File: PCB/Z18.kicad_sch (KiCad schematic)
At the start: 193 parts, among them J1 C165948_-_USB_C_Receptacle_US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, J2 SM02B-SRSS-TB(LF)(SN), J3 SM02B-SRSS-TB(LF)(SN), J4 Conn_ARM_JTAG_SWD_10, Q1 Q_PMOS_GSD, SW1 CAP_STP, SW10 A, SW11 WIN_1.25U, SW12 2, SW13 W, SW14 S, SW15 Z, SW16 L_ALT_1.25U, SW17 L_ALT_1.5U, SW18 3, SW19 E, SW2 ESC, SW20 D, SW21 X, SW22 4, SW23 R, SW24 F, SW25 C, SW26 5, SW27 T, SW28 G, SW29 V, SW3 Tab, SW30 SPC_6.25U, SW31 SPC_7U, SW32 6, SW33 Y, SW34 H, SW35 B, SW36 7, SW37 U, SW38 J, SW39 N, SW4 CAP, SW40 8, SW41 I, SW42 K, SW43 M, SW44 R_ALT_1U, SW45 R_ALT_1.5U, SW46 9, SW47 O, SW48 L, SW49 ,, SW5 L_SHFT, SW50 R_WIN_1U, SW51 R_CTRL_1.5U, SW52 0, SW53 P, SW54 ;, SW55 ., SW56 R_CTRL_1U, SW57 -, SW58 [, SW59 ', SW6 L_CTRL_1.25U, SW60 /, SW61 =, SW62 ], SW63 R_SHFT_1.75U, SW64 LEFT, SW65 Rotary_Encoder_Switch-Device-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, SW66 BCKSP, SW67 \, SW68 ENT, SW69 UP, SW7 L_CTRL_1.5U, SW70 DOWN, SW71 ENT_ISO, SW72 Tilde, SW73 Del, SW74 PG_UP, SW75 PG_DWN, SW76 RIGHT, SW77 ISO_SPARE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

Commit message: starting updates, incomplete
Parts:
- removed C1, C3: 10uF, Capacitor_SMD:C_0603_1608Metric, symbol Device:C_Small
- added D? (x13): D, Diode_SMD:D_SOD-123, symbol Device:D_Small
- added SW?: np_9, Button_Switch_Keyboard:SW_Cherry_MX_1.00u_PCB, symbol Switch:SW_Push
- added SW?: np_0, Button_Switch_Keyboard:SW_Cherry_MX_1.00u_PCB, symbol Switch:SW_Push
- added SW?: np_minus, Button_Switch_Keyboard:SW_Cherry_MX_1.00u_PCB, symbol Switch:SW_Push
- added SW?: np_3, Button_Switch_Keyboard:SW_Cherry_MX_1.00u_PCB, symbol Switch:SW_Push
- added SW?: np_5, Button_Switch_Keyboard:SW_Cherry_MX_1.00u_PCB, symbol Switch:SW_Push
- added SW?: np_ent, Button_Switch_Keyboard:SW_Cherry_MX_1.00u_PCB, symbol Switch:SW_Push
- added SW?: np_2, Button_Switch_Keyboard:SW_Cherry_MX_1.00u_PCB, symbol Switch:SW_Push
- added SW?: np_plus, Button_Switch_Keyboard:SW_Cherry_MX_1.00u_PCB, symbol Switch:SW_Push
- added SW?: np_/, Button_Switch_Keyboard:SW_Cherry_MX_1.00u_PCB, symbol Switch:SW_Push
- added SW?: np_dot, Button_Switch_Keyboard:SW_Cherry_MX_1.00u_PCB, symbol Switch:SW_Push
- added SW?: np_6, Button_Switch_Keyboard:SW_Cherry_MX_1.00u_PCB, symbol Switch:SW_Push
- added SW?: np_8, Button_Switch_Keyboard:SW_Cherry_MX_1.00u_PCB, symbol Switch:SW_Push
- added SW?: np_star, Button_Switch_Keyboard:SW_Cherry_MX_1.00u_PCB, symbol Switch:SW_Push
- SW72: value Tilde -> np_del
- SW74: value PG_UP -> np_4
- SW75: value PG_DWN -> np1
- U3: footprint RF_Module:Raytac_MDBT50Q -> COBoards:E73-2G4M08S1C; symbol RF_Module:MDBT50Q-1MV2 -> COBoards:E73-2G4M08S1C; LCSC PN (none) -> C356849; Manufacturer PN (none) -> E73-2G4M08S1C
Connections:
- net BATTERY_MEASURE: no longer U3.20 (P0.04/AIN2)
- net BOOT_LED: no longer U3.50 (P1.02)
- net Col0: no longer U3.3 (P1.10)
- net Col1: no longer U3.4 (P1.11)
- net Col10: no longer U3.13 (P0.28/AIN4)
- net Col11: no longer U3.14 (P0.30/AIN6)
- net Col12: no longer U3.22 (P0.06)
- net Col13: no longer U3.24 (P0.08)
- net Col14: no longer U3.26 (TRACEDATA3/P1.09)
- net Col2: no longer U3.5 (P1.12)
- net Col3: no longer U3.6 (P1.13)
- net Col4: no longer U3.7 (P1.14)
- net Col5: no longer U3.8 (P1.15)
- net Col6: no longer U3.9 (P0.03/AIN1)
- net Col7: no longer U3.10 (P0.29/AIN5)
- net Col8: no longer U3.11 (P0.02/AIN0)
- net Col9: no longer U3.12 (P0.31/AIN7)
- net D+: now also U3.31 (D+)
- net D-: now also U3.29 (D-)
- net GND: now also U3.21 (GND), U3.24 (GND); no longer U3.1 (GND), U3.15 (GND), U3.2 (GND), U3.33 (GND), U3.55 (GND)
- net RESET: now also U3.26 (P0.18/RESET); no longer U3.40 (~RESET~/P0.18)
- net Row0: now also D?.1 (K), D?.1 (K), D?.1 (K); no longer U3.60 (P1.03)
- net Row1: now also D?.1 (K), D?.1 (K), D?.1 (K); no longer U3.59 (P1.05)
- net Row2: now also D?.1 (K), D?.1 (K); no longer U3.58 (P1.07)
- net Row3: now also D?.1 (K), D?.1 (K), D?.1 (K); no longer U3.57 (P1.06)
- net Row4: now also D?.1 (K), D?.1 (K); no longer U3.56 (P1.04)
- net SWC: now also U3.39 (SWDCLK); no longer U3.53 (SWDCLK)
- net SWD: now also U3.37 (SWDIO); no longer U3.51 (SWDIO)
- net VBUS: now also U3.27 (VBUS); no longer U3.32 (VBUS)
- net VDD: now also U3.19 (VDD), U3.23 (VDDH); no longer U3.28 (VDD), U3.30 (VDDH)
- net at R9.2: no longer U3.34 (D-)
- net at C6.2, Y1.1: now also U3.13 (P0.01/XL2); no longer U3.17 (XL1/P0.00)
- net at C7.2, Y1.2: now also U3.11 (P0.00/XL1); no longer U3.18 (XL2/P0.01)
- net DCCH: now reaches U3.25 (DCCH)
- net at U3.35 (P0.24): no longer R10.2
- net at U3.41 (P0.09/NFC1): no longer TP1.1
- net at TP2.1: no longer U3.44 (P0.20)
- net at TP3.1: no longer U3.46 (P0.22)
- new net: D?.2 (A), SW?.2 (x13)
- new net Col15: SW?.1, SW?.1, SW?.1, SW?.1, SW?.1
- new net Col16: SW?.1, SW?.1, SW?.1, SW?.1, SW?.1
- new net Col17: SW?.1, SW?.1, SW?.1
- no-connect marks 34 -> 20
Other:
- moved on the sheet: BATT1, C2, C5, C6, C7, D1, D2, J1, Q1, R11, R3, R4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

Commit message: layout and routing in progress, ~70% complete
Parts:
- removed D72: D, Diode_SMD:D_SOD-123, symbol Device:D_Small
- removed H2, H3, H4, H5: MountingHole_Pad, MountingHole:MountingHole_2.2mm_M2, symbol Mechanical:MountingHole_Pad
- removed J4: Conn_ARM_JTAG_SWD_10, Connector:Tag-Connect_TC2030-IDC-NL_2x03_P1.27mm_Vertical, symbol Connector:Conn_ARM_JTAG_SWD_10
- removed R10, R9: 27R, Resistor_SMD:R_0603_1608Metric, symbol Device:R_Small
- removed SW31: SPC_7U, COBoards:MX_7U, symbol Switch:SW_Push
- removed SW65: Rotary_Encoder_Switch-Device-SofleKeyboard-rescue, symbol COBoards:Rotary_Encoder_Switch-Device-SofleKeyboard-rescue
- removed SW71: ENT_ISO, Button_Switch_Keyboard:SW_Cherry_MX_ISOEnter_PCB, symbol Switch:SW_Push
- removed SW77: ISO_SPARE, Button_Switch_Keyboard:SW_Cherry_MX_1.00u_PCB, symbol Switch:SW_Push
- removed TP1, TP2, TP3: TestPoint, TestPoint:TestPoint_Pad_1.0x1.0mm, symbol Connector:TestPoint
- added H13: MountingHole_Pad, MountingHole:MountingHole_4.3mm_M4, symbol Mechanical:MountingHole_Pad
- added J5: Conn_01x04_Male, Connector_PinHeader_2.54mm:PinHeader_1x04_P2.54mm_Vertical, symbol Connector:Conn_01x04_Male
- SW1: renamed from SW2; footprint Button_Switch_Keyboard:SW_Cherry_MX_1.00u_PCB -> COBoards:MX_1U
- SW10: renamed from SW46; footprint Button_Switch_Keyboard:SW_Cherry_MX_1.00u_PCB -> COBoards:MX_1U
- SW11: renamed from SW52; footprint Button_Switch_Keyboard:SW_Cherry_MX_1.00u_PCB -> COBoards:MX_1U
- SW12: renamed from SW57; footprint Button_Switch_Keyboard:SW_Cherry_MX_1.00u_PCB -> COBoards:MX_1U
- SW13: renamed from SW61; footprint Button_Switch_Keyboard:SW_Cherry_MX_1.00u_PCB -> COBoards:MX_1U
- SW14: renamed from SW66; footprint Button_Switch_Keyboard:SW_Cherry_MX_2.00u_PCB -> COBoards:MX_2U
- SW15: renamed from SW72; footprint Button_Switch_Keyboard:SW_Cherry_MX_1.00u_PCB -> COBoards:MX_1U
- SW16, SW17, SW18, SW34, SW35, SW54, SW55, SW70, SW71, SW83, SW84: renamed from SW?; footprint Button_Switch_Keyboard:SW_Cherry_MX_1.00u_PCB -> COBoards:MX_1U
- SW19: renamed from SW3; footprint Button_Switch_Keyboard:SW_Cherry_MX_1.50u_PCB -> COBoards:MX_1.5U
- SW2: renamed from SW8; footprint Button_Switch_Keyboard:SW_Cherry_MX_1.00u_PCB -> COBoards:MX_1U
- SW20: renamed from SW9; footprint Button_Switch_Keyboard:SW_Cherry_MX_1.00u_PCB -> COBoards:MX_1U
- SW21: renamed from SW13; footprint Button_Switch_Keyboard:SW_Cherry_MX_1.00u_PCB -> COBoards:MX_1U
- SW22: renamed from SW19; footprint Button_Switch_Keyboard:SW_Cherry_MX_1.00u_PCB -> COBoards:MX_1U
- SW23, SW48: footprint Button_Switch_Keyboard:SW_Cherry_MX_1.00u_PCB -> COBoards:MX_1U
- SW24: renamed from SW27; footprint Button_Switch_Keyboard:SW_Cherry_MX_1.00u_PCB -> COBoards:MX_1U
- SW25: renamed from SW33; footprint Button_Switch_Keyboard:SW_Cherry_MX_1.00u_PCB -> COBoards:MX_1U
- SW26: renamed from SW37; footprint Button_Switch_Keyboard:SW_Cherry_MX_1.00u_PCB -> COBoards:MX_1U
- SW27: renamed from SW41; footprint Button_Switch_Keyboard:SW_Cherry_MX_1.00u_PCB -> COBoards:MX_1U
- SW28: renamed from SW47; footprint Button_Switch_Keyboard:SW_Cherry_MX_1.00u_PCB -> COBoards:MX_1U
- SW29: renamed from SW53; footprint Button_Switch_Keyboard:SW_Cherry_MX_1.00u_PCB -> COBoards:MX_1U
- SW3: renamed from SW12; footprint Button_Switch_Keyboard:SW_Cherry_MX_1.00u_PCB -> COBoards:MX_1U
- SW30: renamed from SW58; footprint Button_Switch_Keyboard:SW_Cherry_MX_1.00u_PCB -> COBoards:MX_1U
- SW31: renamed from SW62; footprint Button_Switch_Keyboard:SW_Cherry_MX_1.00u_PCB -> COBoards:MX_1U
- SW32: renamed from SW67; footprint Button_Switch_Keyboard:SW_Cherry_MX_1.50u_PCB -> COBoards:MX_1.5U
- SW33: renamed from SW73; value Del -> np_7; footprint Button_Switch_Keyboard:SW_Cherry_MX_1.00u_PCB -> COBoards:MX_1U
- SW36, SW72: renamed from SW?; footprint Button_Switch_Keyboard:SW_Cherry_MX_1.00u_PCB -> COBoards:MX_2U
- SW39: renamed from SW4; footprint Button_Switch_Keyboard:SW_Cherry_MX_1.75u_PCB -> COBoards:MX_1.75U
- SW4: renamed from SW18; footprint Button_Switch_Keyboard:SW_Cherry_MX_1.00u_PCB -> COBoards:MX_1U
- SW40: renamed from SW10; footprint Button_Switch_Keyboard:SW_Cherry_MX_1.00u_PCB -> COBoards:MX_1U
- SW41: renamed from SW14; footprint Button_Switch_Keyboard:SW_Cherry_MX_1.00u_PCB -> COBoards:MX_1U
- SW42: renamed from SW20; footprint Button_Switch_Keyboard:SW_Cherry_MX_1.00u_PCB -> COBoards:MX_1U
- SW43: renamed from SW24; footprint Button_Switch_Keyboard:SW_Cherry_MX_1.00u_PCB -> COBoards:MX_1U
- SW44: renamed from SW28; footprint Button_Switch_Keyboard:SW_Cherry_MX_1.00u_PCB -> COBoards:MX_1U
- SW45: renamed from SW34; footprint Button_Switch_Keyboard:SW_Cherry_MX_1.00u_PCB -> COBoards:MX_1U
- SW46: renamed from SW38; footprint Button_Switch_Keyboard:SW_Cherry_MX_1.00u_PCB -> COBoards:MX_1U
- SW47: renamed from SW42; footprint Button_Switch_Keyboard:SW_Cherry_MX_1.00u_PCB -> COBoards:MX_1U
- SW49: renamed from SW54; footprint Button_Switch_Keyboard:SW_Cherry_MX_1.00u_PCB -> COBoards:MX_1U
- SW5: renamed from SW22; footprint Button_Switch_Keyboard:SW_Cherry_MX_1.00u_PCB -> COBoards:MX_1U
- SW50: renamed from SW59; footprint Button_Switch_Keyboard:SW_Cherry_MX_1.00u_PCB -> COBoards:MX_1U
- SW52: renamed from SW68; footprint Button_Switch_Keyboard:SW_Cherry_MX_2.25u_PCB -> COBoards:MX_2.25U
- SW53: renamed from SW74; footprint Button_Switch_Keyboard:SW_Cherry_MX_1.00u_PCB -> COBoards:MX_1U
- SW56: renamed from SW5; footprint Button_Switch_Keyboard:SW_Cherry_MX_2.25u_PCB -> COBoards:MX_2.25U
- SW57: renamed from SW15; footprint Button_Switch_Keyboard:SW_Cherry_MX_1.00u_PCB -> COBoards:MX_1U
- SW58: renamed from SW21; footprint Button_Switch_Keyboard:SW_Cherry_MX_1.00u_PCB -> COBoards:MX_1U
- SW59: renamed from SW25; footprint Button_Switch_Keyboard:SW_Cherry_MX_1.00u_PCB -> COBoards:MX_1U
- SW6: renamed from SW26; footprint Button_Switch_Keyboard:SW_Cherry_MX_1.00u_PCB -> COBoards:MX_1U
- SW60: renamed from SW29; footprint Button_Switch_Keyboard:SW_Cherry_MX_1.00u_PCB -> COBoards:MX_1U
- SW61: renamed from SW35; footprint Button_Switch_Keyboard:SW_Cherry_MX_1.00u_PCB -> COBoards:MX_1U
- SW62: renamed from SW39; footprint Button_Switch_Keyboard:SW_Cherry_MX_1.00u_PCB -> COBoards:MX_1U
- SW63: renamed from SW43; footprint Button_Switch_Keyboard:SW_Cherry_MX_1.00u_PCB -> COBoards:MX_1U
- SW64: renamed from SW49; footprint Button_Switch_Keyboard:SW_Cherry_MX_1.00u_PCB -> COBoards:MX_1U
- SW65: renamed from SW55; footprint Button_Switch_Keyboard:SW_Cherry_MX_1.00u_PCB -> COBoards:MX_1U
- SW66: renamed from SW60; footprint Button_Switch_Keyboard:SW_Cherry_MX_1.00u_PCB -> COBoards:MX_1U
- SW67: renamed from SW63; footprint Button_Switch_Keyboard:SW_Cherry_MX_1.75u_PCB -> COBoards:MX_1.75U
- SW68: renamed from SW69; footprint Button_Switch_Keyboard:SW_Cherry_MX_1.00u_PCB -> COBoards:MX_1U
- SW69: renamed from SW75; footprint Button_Switch_Keyboard:SW_Cherry_MX_1.00u_PCB -> COBoards:MX_1U
- SW7: renamed from SW32; footprint Button_Switch_Keyboard:SW_Cherry_MX_1.00u_PCB -> COBoards:MX_1U
- SW73: renamed from SW6; footprint Button_Switch_Keyboard:SW_Cherry_MX_1.25u_PCB -> COBoards:MX_1.25U
- SW74: renamed from SW11; footprint Button_Switch_Keyboard:SW_Cherry_MX_1.25u_PCB -> COBoards:MX_1.25U
- SW75: renamed from SW16; footprint Button_Switch_Keyboard:SW_Cherry_MX_1.25u_PCB -> COBoards:MX_1.25U
- SW76: renamed from SW30; footprint Button_Switch_Keyboard:SW_Cherry_MX_6.25u_PCB -> COBoards:MX_6.25U
- SW77: renamed from SW44; footprint Button_Switch_Keyboard:SW_Cherry_MX_1.00u_PCB -> COBoards:MX_1U
- SW78: renamed from SW50; footprint Button_Switch_Keyboard:SW_Cherry_MX_1.00u_PCB -> COBoards:MX_1U
- SW79: renamed from SW56; footprint Button_Switch_Keyboard:SW_Cherry_MX_1.00u_PCB -> COBoards:MX_1U
- SW8: renamed from SW36; footprint Button_Switch_Keyboard:SW_Cherry_MX_1.00u_PCB -> COBoards:MX_1U
- SW80: renamed from SW64; footprint Button_Switch_Keyboard:SW_Cherry_MX_1.00u_PCB -> COBoards:MX_1U
- SW81: renamed from SW70; footprint Button_Switch_Keyboard:SW_Cherry_MX_1.00u_PCB -> COBoards:MX_1U
- SW82: renamed from SW76; footprint Button_Switch_Keyboard:SW_Cherry_MX_1.00u_PCB -> COBoards:MX_1U
- SW85: renamed from SW51; footprint Button_Switch_Keyboard:SW_Cherry_MX_1.50u_PCB -> COBoards:MX_1.5U
- SW86: renamed from SW7; footprint Button_Switch_Keyboard:SW_Cherry_MX_1.50u_PCB -> COBoards:MX_1.5U
- SW87: renamed from SW17; footprint Button_Switch_Keyboard:SW_Cherry_MX_1.50u_PCB -> COBoards:MX_1.5U
- SW9: renamed from SW40; footprint Button_Switch_Keyboard:SW_Cherry_MX_1.00u_PCB -> COBoards:MX_1U
- gave numbers to parts that had none: 13
- renumbered C6 to C1, C7 to C2, C4 to C3, C5 to C4, C2 to C5, D4 to D1, D44 to D10, D49 to D11, D54 to D12, D58 to D13, D62 to D14, D67 to D15, D5 to D19, D9 to D2, D10 to D20, D14 to D21, D19 to D22, D27 to D24, D32 to D25, D36 to D26, D40 to D27, D45 to D28, D50 to D29, D13 to D3, D55 to D30, D59 to D31, D63 to D32, D68 to D33, D6 to D37, D11 to D38, D15 to D39, D18 to D4, D20 to D40, D24 to D41, D28 to D42, D33 to D43, D37 to D44, D41 to D45, D51 to D47, D56 to D48, D22 to D5, D64 to D50, D69 to D51, D7 to D54, D16 to D55, D21 to D56, D25 to D57, D29 to D58, D34 to D59, D26 to D6, D38 to D60, D42 to D61, D47 to D62, D52 to D63, D57 to D64, D60 to D65, D65 to D66, D70 to D67, D31 to D7, D8 to D71, D12 to D72, D17 to D73, D30 to D74, D43 to D75, D48 to D76, D53 to D77, D61 to D78, D66 to D79, D35 to D8, D71 to D80, D3 to D83, D2 to D85, D1 to D86, D39 to D9, H9 to H10, H10 to H11, H6 to H3, H11 to H5, H8 to H7, H7 to H9, J1 to J4, R6 to R1, R1 to R2, R2 to R3, R8 to R4, R3 to R5, R4 to R6, R11 to R8, R5 to R9, SW1 to SW38, SW45 to SW89, U3 to U2, U2 to U3
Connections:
- net Col10 is gone; now on net Col5: SW11.1, SW29.1, SW49.1, SW65.1, SW79.1, SW85.1
- net Col11 is gone; now on net Col5: SW12.1, SW30.1, SW50.1, SW66.1
- net Col12 is gone; now on net Col6: SW13.1, SW31.1, SW67.1, SW80.1
- net Col13 is gone; now on net Col6: SW14.1, SW32.1, SW52.1, SW68.1, SW81.1
- net Col14 is gone; now on net Col7: SW15.1, SW33.1, SW53.1, SW69.1, SW82.1
- net Col15 is gone; now on net Col7: SW16.1, SW34.1, SW54.1, SW70.1, SW83.1
- net Col16 is gone; now on net Col8: SW17.1, SW35.1, SW55.1, SW71.1, SW84.1
- net Col17 is gone; now on net Col8: SW18.1, SW36.1, SW72.1
- net BATTERY_MEASURE: now also U2.10 (P0.30/AIN6_(LowFreq))
- net BOOT_LED: now also U2.9 (P0.31/AIN7_(LowFreq))
- net Col0: now also SW2.1, SW20.1, SW40.1, SW74.1, U2.1 (P1.11)
- net Col1: now also SW21.1, SW22.1, SW3.1, SW4.1, SW41.1, SW42.1, SW57.1, SW58.1, SW75.1, SW87.1, U2.2 (P1.10_(LowFreq)); no longer SW2.1, SW20.1, SW40.1, SW74.1
- net Col2: now also SW23.1, SW24.1, SW43.1, SW44.1, SW5.1, SW59.1, SW6.1, SW60.1, SW76.1, U2.3 (P0.03/AIN1_(LowFreq)); no longer SW21.1, SW3.1, SW41.1, SW57.1, SW75.1, SW87.1
- net Col3: now also SW25.1, SW26.1, SW45.1, SW46.1, SW61.1, SW62.1, SW7.1, SW8.1, U2.4 (P0.28/AIN4); no longer SW22.1, SW4.1, SW42.1, SW58.1
- net Col4: now also SW10.1, SW27.1, SW28.1, SW47.1, SW48.1, SW63.1, SW64.1, SW77.1, SW89.1, SW9.1, U2.6 (P1.13_(LowFreq)); no longer SW23.1, SW43.1, SW5.1, SW59.1
- net Col5: now also SW78.1, U2.8 (P0.29/AIN5_(LowFreq)); no longer SW24.1, SW44.1, SW6.1, SW60.1, SW76.1
- net Col6: now also U2.7 (P0.02/AIN0_(LowFreq)); no longer SW25.1, SW45.1, SW61.1, SW7.1
- net Col7: now also U2.15 (P0.05/AIN3); no longer SW26.1, SW46.1, SW62.1, SW8.1
- net Col8: now also U2.17 (P1.09); no longer SW27.1, SW47.1, SW63.1, SW77.1, SW89.1, SW9.1
- net GND: now also U2.5 (GND), J5.1 (Pin_1)
- net Row0: now also U2.43 (P0.10/NFC2)
- net Row1: now also U2.41 (P0.09/NFC1)
- net Row2: now also U2.35 (P0.24)
- net Row3: now also U2.33 (P0.13)
- net Row4: now also U2.12 (P0.26)
- net SWC: now also J5.4 (Pin_4)
- net SWD: now also J5.3 (Pin_3)
- removed net Col9: SW10.1, SW28.1, SW48.1, SW64.1, SW78.1
- no-connect marks 20 -> 26
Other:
- moved on the sheet: BATT1, C1, C2, C4, C5, D75, D76, D77, D85, D86, J3, J4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

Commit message: routed
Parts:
- removed SW86: L_CTRL_1.5U, COBoards:MX_1.5U, symbol Switch:SW_Push
- removed SW87: L_ALT_1.5U, COBoards:MX_1.5U, symbol Switch:SW_Push
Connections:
- net Col0: now also U2.2 (P1.10_(LowFreq)); no longer U2.1 (P1.11)
- net Col1: now also U2.1 (P1.11); no longer U2.2 (P1.10_(LowFreq))
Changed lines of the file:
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@@
     (stroke (width 0) (type solid) (color 0 0 0 0))
   )
-  (wire (pts (xy 46.99 114.3) (xy 46.99 102.87))
-    (stroke (width 0) (type solid) (color 0 0 0 0))
-  )
   (wire (pts (xy 200.66 40.64) (xy 200.66 55.88))
     (stroke (width 0) (type solid) (color 0 0 0 0))
@@
     (stroke (width 0) (type solid) (color 0 0 0 0))
   )
-  (wire (pts (xy 77.47 114.3) (xy 77.47 101.6))
-    (stroke (width 0) (type solid) (color 0 0 0 0))
-  )
   (wire (pts (xy 40.64 66.04) (xy 40.64 71.12))
     (stroke (width 0) (type solid) (color 0 0 0 0))
@@
     (stroke (width 0) (type solid) (color 0 0 0 0))
   )
-  (wire (pts (xy 87.63 101.6) (xy 87.63 114.3))
-    (stroke (width 0) (type solid) (color 0 0 0 0))
-  )
   (wire (pts (xy 71.12 142.24) (xy 71.12 139.7))
     (stroke (width 0) (type solid) (color 0 0 0 0))
@@
     (stroke (width 0) (type default) (color 0 0 0 0))
   )
-  (wire (pts (xy 57.15 101.6) (xy 57.15 114.3))
-    (stroke (width 0) (type solid) (color 0 0 0 0))
-  )
   (wire (pts (xy 185.42 86.36) (xy 185.42 101.6))
     (stroke (width 0) (type default) (color 0 0 0 0))
@@
     (effects (font (size 1.27 1.27)) (justify right bottom))
   )
-  (label "Col1" (at 85.09 220.98 0)
+  (label "Col1" (at 85.09 223.52 0)
     (effects (font (size 1.27 1.27)) (justify left bottom))
   )
@@
     (effects (font (size 1.27 1.27)) (justify left bottom))
   )
-  (label "Col0" (at 85.09 223.52 0)
+  (label "Col0" (at 85.09 220.98 0)
     (effects (font (size 1.27 1.27)) (justify left bottom))
   )
@@
     (pin "2")
   )
-  (symbol (lib_id "Switch:SW_Push") (at 52.07 114.3 0) (unit 1)
-    (in_bom yes) (on_board yes)
-    (property "Reference" "SW86" (id 0) (at 52.07 109.7088 0))
-    (property "Value" "L_CTRL_1.5U" (id 1) (at 50.165 112.008 0))
-    (property "Footprint" "COBoards:MX_1.5U" (id 2) (at 52.07 109.22 0)
-      (effects (font (size 1.27 1.27)) hide)
-    )
-    (property "Datasheet" "~" (id 3) (at 52.07 109.22 0)
-      (effects (font (size 1.27 1.27)) hide)
-    )
-    (pin "1")
-    (pin "2")
-  )
   (symbol (lib_id "COBoards:E73-2G4M08S1C") (at 57.15 210.82 0) (unit 1)
     (in_bom yes) (on_board yes)
@@
     (pin "2")
   )
-  (symbol (lib_id "Switch:SW_Push") (at 82.55 114.3 0) (unit 1)
-    (in_bom yes) (on_board yes)
-    (property "Reference" "SW87" (id 0) (at 82.55 109.7088 0))
-    (property "Value" "L_ALT_1.5U" (id 1) (at 80.645 112.008 0))
-    (property "Footprint" "COBoards:MX_1.5U" (id 2) (at 82.55 109.22 0)
-      (effects (font (size 1.27 1.27)) hide)
-    )
-    (property "Datasheet" "~" (id 3) (at 82.55 109.22 0)
-      (effects (font (size 1.27 1.27)) hide)
-    )
-    (pin "1")
-    (pin "2")
-  )
   (symbol (lib_id "Mechanical:MountingHole_Pad") (at 353.06 201.93 0) (unit 1)
     (in_bom yes) (on_board yes)
@@
       (reference "SW85") (unit 1) (value "R_CTRL_1.5U") (footprint "COBoards:MX_1.5U")
     )
-    (path "/2b04a5df-fab2-471c-89c8-d8e5ba4981b5"
-      (reference "SW86") (unit 1) (value "L_CTRL_1.5U") (footprint "COBoards:MX_1.5U")
-    )
-    (path "/9d1ebf75-7a38-4026-b965-5f1c50ad330c"
-      (reference "SW87") (unit 1) (value "L_ALT_1.5U") (footprint "COBoards:MX_1.5U")
-    )
     (path "/0921978f-5ad5-471e-8955-073e12610353"

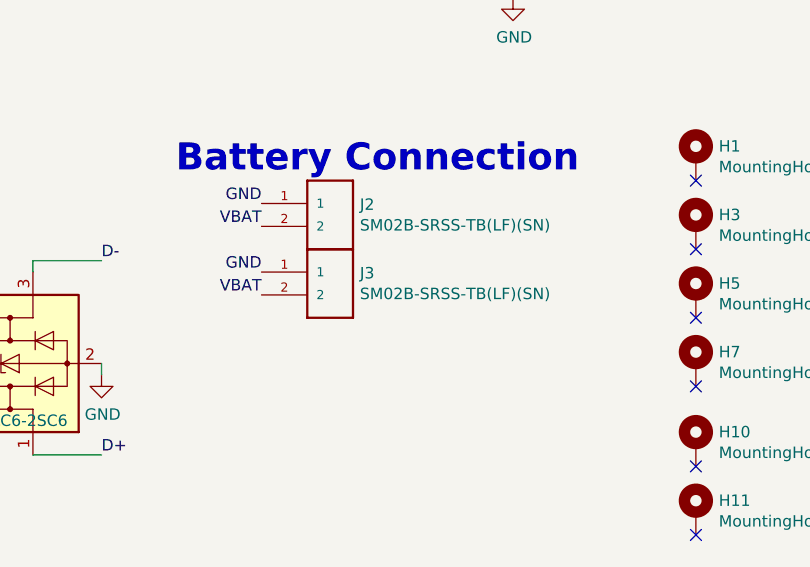
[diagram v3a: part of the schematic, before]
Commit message: update to fix step export issue, cleanup footprint and symbol references
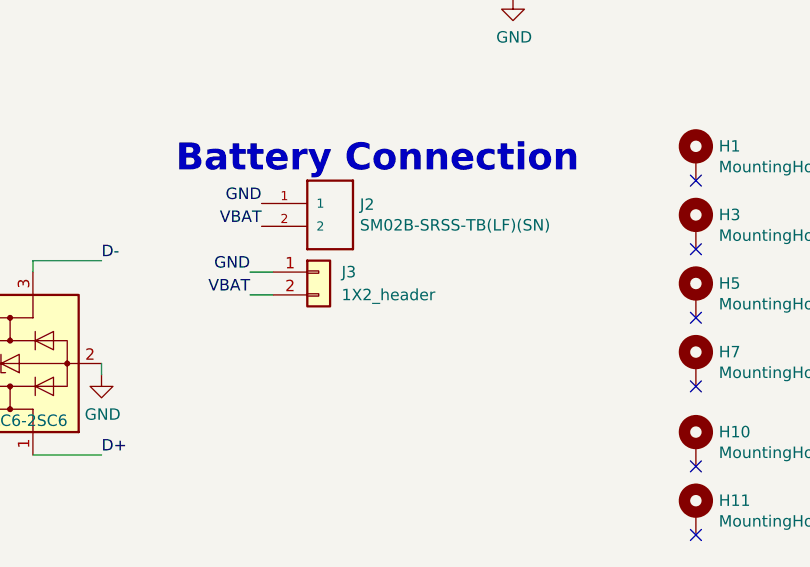
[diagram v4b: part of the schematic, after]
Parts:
- J3: value SM02B-SRSS-TB(LF)(SN) -> 1X2_header; symbol SM02B-SRSS-TB_LF__SN_:SM02B-SRSS-TB(LF)(SN) -> Connector_Generic:Conn_01x02
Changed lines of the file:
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@@
     (stroke (width 0) (type solid) (color 0 0 0 0))
   )
+  (wire (pts (xy 303.53 214.63) (xy 306.07 214.63))
+    (stroke (width 0) (type default) (color 0 0 0 0))
+  )
   (wire (pts (xy 101.6 60.96) (xy 116.84 60.96))
     (stroke (width 0) (type solid) (color 0 0 0 0))
@@
     (stroke (width 0) (type solid) (color 0 0 0 0))
   )
+  (wire (pts (xy 303.53 217.17) (xy 306.07 217.17))
+    (stroke (width 0) (type default) (color 0 0 0 0))
+  )
   (wire (pts (xy 55.88 91.44) (xy 86.36 91.44))
     (stroke (width 0) (type solid) (color 0 0 0 0))
@@
     (effects (font (size 1.27 1.27)) (justify right bottom))
   )
-  (label "VBAT" (at 304.8 217.17 180)
+  (label "VBAT" (at 303.53 217.17 180)
     (effects (font (size 1.27 1.27)) (justify right bottom))
   )
@@
     (effects (font (size 1.27 1.27)) (justify left bottom))
   )
-  (label "GND" (at 304.8 214.63 180)
+  (label "GND" (at 303.53 214.63 180)
     (effects (font (size 1.27 1.27)) (justify right bottom))
   )
@@
     (pin "2")
   )
-  (symbol (lib_id "SM02B-SRSS-TB_LF__SN_:SM02B-SRSS-TB(LF)(SN)") (at 304.8 219.71 0) (unit 1)
+  (symbol (lib_id "Connector_Generic:Conn_01x02") (at 311.15 214.63 0) (unit 1)
     (in_bom yes) (on_board yes)
-    (property "Reference" "J3" (id 0) (at 315.7221 214.7506 0)
+    (property "Reference" "J3" (id 0) (at 313.69 214.63 0)
       (effects (font (size 1.27 1.27)) (justify left))
     )
-    (property "Value" "SM02B-SRSS-TB(LF)(SN)" (id 1) (at 315.7221 217.0493 0)
+    (property "Value" "1X2_header" (id 1) (at 313.69 217.17 0)
       (effects (font (size 1.27 1.27)) (justify left))
     )
-    (property "Footprint" "Connector_PinHeader_2.54mm:PinHeader_1x02_P2.54mm_Vertical" (id 2) (at 304.8 219.71 0)
-      (effects (font (size 1.27 1.27)) (justify left bottom) hide)
+    (property "Footprint" "Connector_PinHeader_2.54mm:PinHeader_1x02_P2.54mm_Vertical" (id 2) (at 311.15 214.63 0)
+      (effects (font (size 1.27 1.27)) hide)
     )
-    (property "Datasheet" "" (id 3) (at 304.8 219.71 0)
-      (effects (font (size 1.27 1.27)) (justify left bottom) hide)
+    (property "Datasheet" "~" (id 3) (at 311.15 214.63 0)
+      (effects (font (size 1.27 1.27)) hide)
     )
-    (property "MP" "SM02B-SRSS-TB_LF__SN_" (id 4) (at 304.8 219.71 0)
+    (property "MP" "SM02B-SRSS-TB_LF__SN_" (id 4) (at 311.15 214.63 0)
       (effects (font (size 1.27 1.27)) (justify left bottom) hide)
     )
-    (property "AVAILABILITY" "Good" (id 5) (at 304.8 219.71 0)
+    (property "AVAILABILITY" "Good" (id 5) (at 311.15 214.63 0)
       (effects (font (size 1.27 1.27)) (justify left bottom) hide)
     )
-    (property "PRICE" "0.23 USD" (id 6) (at 304.8 219.71 0)
+    (property "PRICE" "0.23 USD" (id 6) (at 311.15 214.63 0)
       (effects (font (size 1.27 1.27)) (justify left bottom) hide)
     )
-    (property "DESCRIPTION" "SH Series 2 Position 1 mm Pitch Surface Mount Side Entry Shrouded Header" (id 7) (at 304.8 219.71 0)
+    (property "DESCRIPTION" "SH Series 2 Position 1 mm Pitch Surface Mount Side Entry Shrouded Header" (id 7) (at 311.15 214.63 0)
       (effects (font (size 1.27 1.27)) (justify left bottom) hide)
     )
-    (property "MF" "JST" (id 8) (at 304.8 219.71 0)
+    (property "MF" "JST" (id 8) (at 311.15 214.63 0)
       (effects (font (size 1.27 1.27)) (justify left bottom) hide)
     )
-    (property "PACKAGE" "None" (id 9) (at 304.8 219.71 0)
+    (property "PACKAGE" "None" (id 9) (at 311.15 214.63 0)
       (effects (font (size 1.27 1.27)) (justify left bottom) hide)
     )
@@
     )
     (path "/70b5bca1-0b96-4ac4-a51e-5aa21489f7ca"
-      (reference "J3") (unit 1) (value "SM02B-SRSS-TB(LF)(SN)") (footprint "Connector_PinHeader_2.54mm:PinHeader_1x02_P2.54mm_Vertical")
+      (reference "J3") (unit 1) (value "1X2_header") (footprint "Connector_PinHeader_2.54mm:PinHeader_1x02_P2.54mm_Vertical")
     )
     (path "/828ef4a2-7b85-44c5-b8f5-7943f2969d3f"

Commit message: JLC rev1 order placed
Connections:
- no-connect marks 26 -> 25
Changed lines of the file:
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@@
   (no_connect (at 166.37 208.28))
   (no_connect (at 353.06 219.71))
-  (no_connect (at 40.64 54.61))
   (no_connect (at 48.26 175.26))
   (no_connect (at 68.58 175.26))
